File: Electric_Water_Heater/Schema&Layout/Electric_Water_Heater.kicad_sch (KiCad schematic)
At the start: 12 parts, among them J1 Barrel_Jack_Switch, U1 ATmega32A-P, U2 L7805, Y1 16MHz

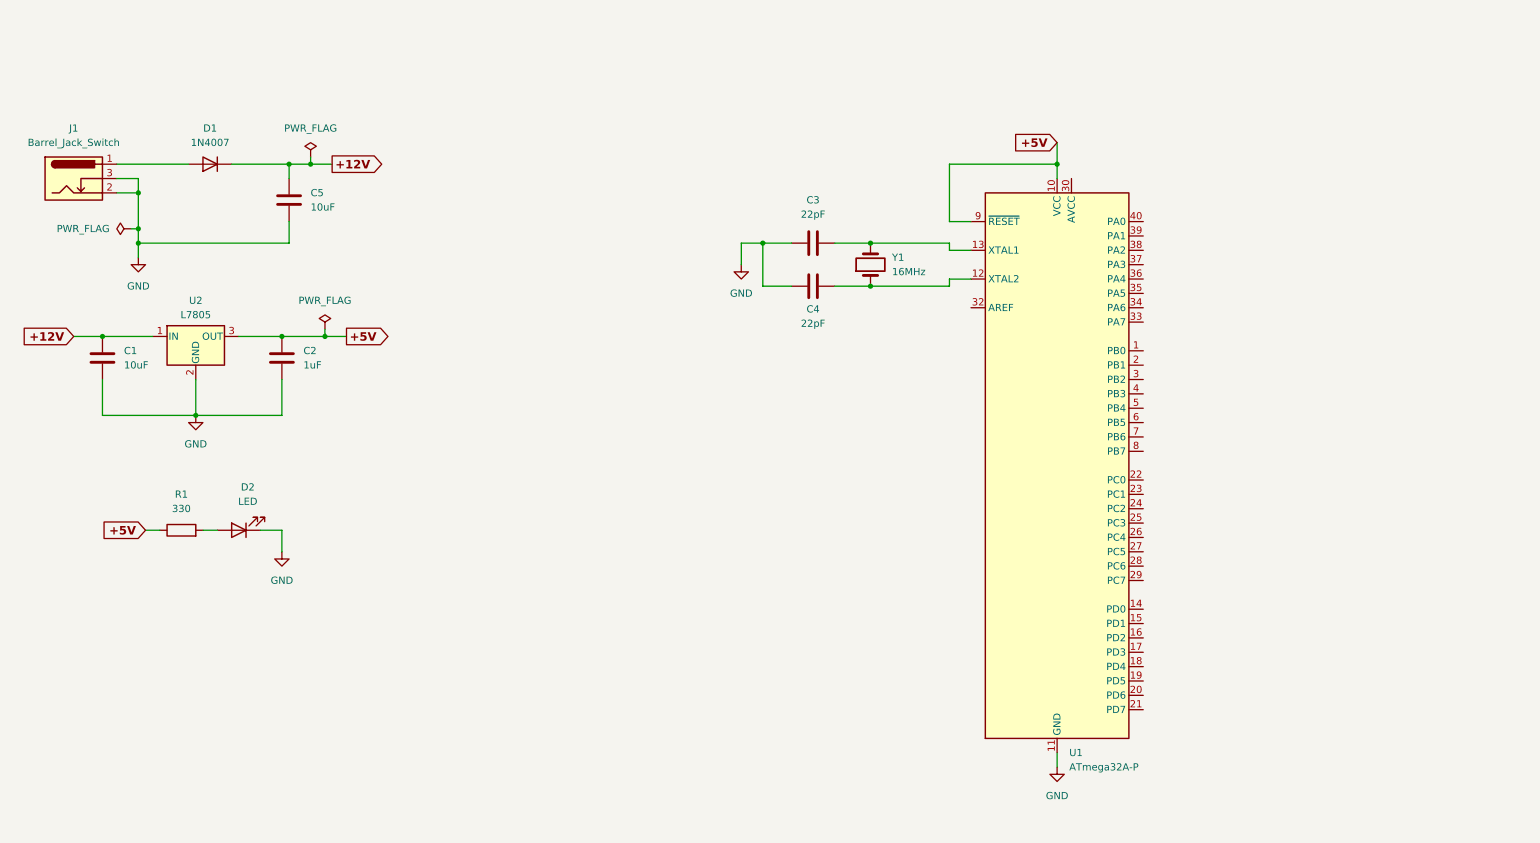
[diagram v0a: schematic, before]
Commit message: Interrupt Added
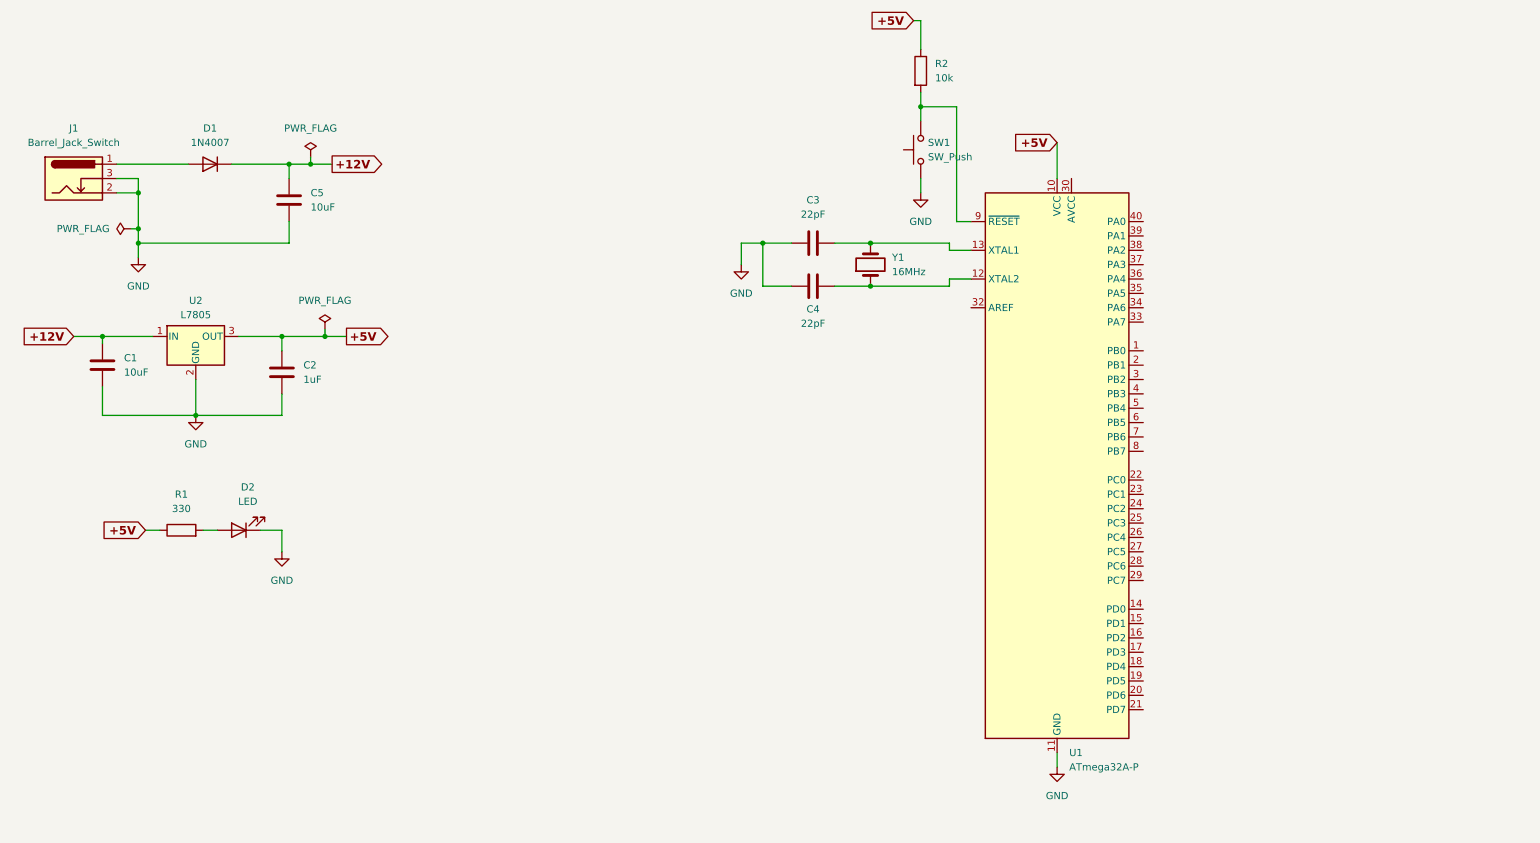
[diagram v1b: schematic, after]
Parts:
- added R2: 10k, symbol Device:R
- added SW1: SW_Push, symbol Switch:SW_Push
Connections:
- net +5V: now also R2.1; no longer U1.9 (~{RESET})
- net GND: now also SW1.1
- new net: R2.2, SW1.2, U1.9 (~{RESET})
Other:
- moved on the sheet: C1, C2

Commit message: New_Update
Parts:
- added R10, R11: 4.7K, symbol Device:R
- added R3, R4, R5, R6, R7, R8, R9: 220, symbol Device:R
- added U3: 7447, Decoder:7447, symbol 74xx_IEEE:7447
- added U4: ELD-426SYGWA, Display_7Segment:ELD_426XXXX, symbol Display_Character:ELD-426SYGWA
- added U5: ST24C08, Memory:ST24C08, symbol Memory_EEPROM:ST24C08
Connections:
- net +5V: now also R10.2, R11.1, U3.16 (VCC), U3.3 (~{LT}), U3.4 (~{BI}), U3.5 (~{RBI}), U5.8 (VCC)
- net GND: now also U3.8 (GND), U5.1 (PRE), U5.3 (E), U5.4 (GND), U5.7 (WP)
- net PD6: now reaches U1.20 (PD6)
- net PD6: now also U4.10 (CA_D1)
- net PD7: now reaches U1.21 (PD7)
- net PD7: now also U4.5 (CA_D2)
- net PC0: now reaches U1.22 (PC0)
- net PC0: now also R10.1, U5.6 (SCL)
- net PC1: now reaches U1.23 (PC1)
- net PC1: now also R11.2, U5.5 (SDA)
- net PB4: now reaches U1.5 (PB4)
- net PB4: now also U3.7 (A)
- net PB5: now reaches U1.6 (PB5)
- net PB5: now also U3.1 (B)
- net PB6: now reaches U1.7 (PB6)
- net PB6: now also U3.2 (C)
- net PB7: now reaches U1.8 (PB7)
- net PB7: now also U3.6 (D)
- new net: R8.1, U3.15 (~{f})
- new net: R8.2, U4.8 (f)
- new net: R6.1, U3.10 (~{d})
- new net: R5.1, U3.11 (~{c})
- new net: R4.1, U3.12 (~{b})
- new net: R3.1, U3.13 (~{a})
- new net: R9.1, U3.14 (~{g})
- new net: R7.1, U3.9 (~{e})
- new net: R5.2, U4.4 (c)
- new net: R6.2, U4.1 (d)
- new net: R7.2, U4.3 (e)
- new net: R4.2, U4.6 (b)
- new net: R3.2, U4.7 (a)
- new net: R9.2, U4.9 (g)
- no-connect marks 0 -> 1
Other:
- moved on the sheet: C1, C2, C3, C4, C5, D1, D2, J1, R1, R2, SW1, U1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
